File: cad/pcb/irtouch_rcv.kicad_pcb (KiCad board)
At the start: 4 copper layers, 42.8 x 43.1 mm, 106 parts, among them Q1 Q_Photo_NPN, Q10 Q_Photo_NPN, Q11 Q_Photo_NPN, Q12 Q_Photo_NPN, Q13 Q_Photo_NPN, Q14 Q_Photo_NPN, Q15 Q_Photo_NPN, Q16 Q_Photo_NPN, Q17 Q_Photo_NPN, Q18 Q_Photo_NPN, Q19 Q_Photo_NPN, Q2 Q_Photo_NPN, Q20 Q_Photo_NPN, Q21 Q_Photo_NPN, Q22 Q_Photo_NPN, Q23 Q_Photo_NPN, Q24 Q_Photo_NPN, Q25 Q_Photo_NPN, Q26 Q_Photo_NPN, Q27 Q_Photo_NPN, Q28 Q_Photo_NPN, Q29 Q_Photo_NPN, Q3 Q_Photo_NPN, Q30 Q_Photo_NPN, Q31 Q_Photo_NPN, Q32 Q_Photo_NPN, Q4 Q_Photo_NPN, Q5 Q_Photo_NPN, Q6 Q_Photo_NPN, Q7 Q_Photo_NPN, Q8 Q_Photo_NPN, Q9 Q_Photo_NPN, U1 74HC4051PW,118, U2 74HC4051PW,118, U3 74HC4051PW,118, U4 74HC4051PW,118

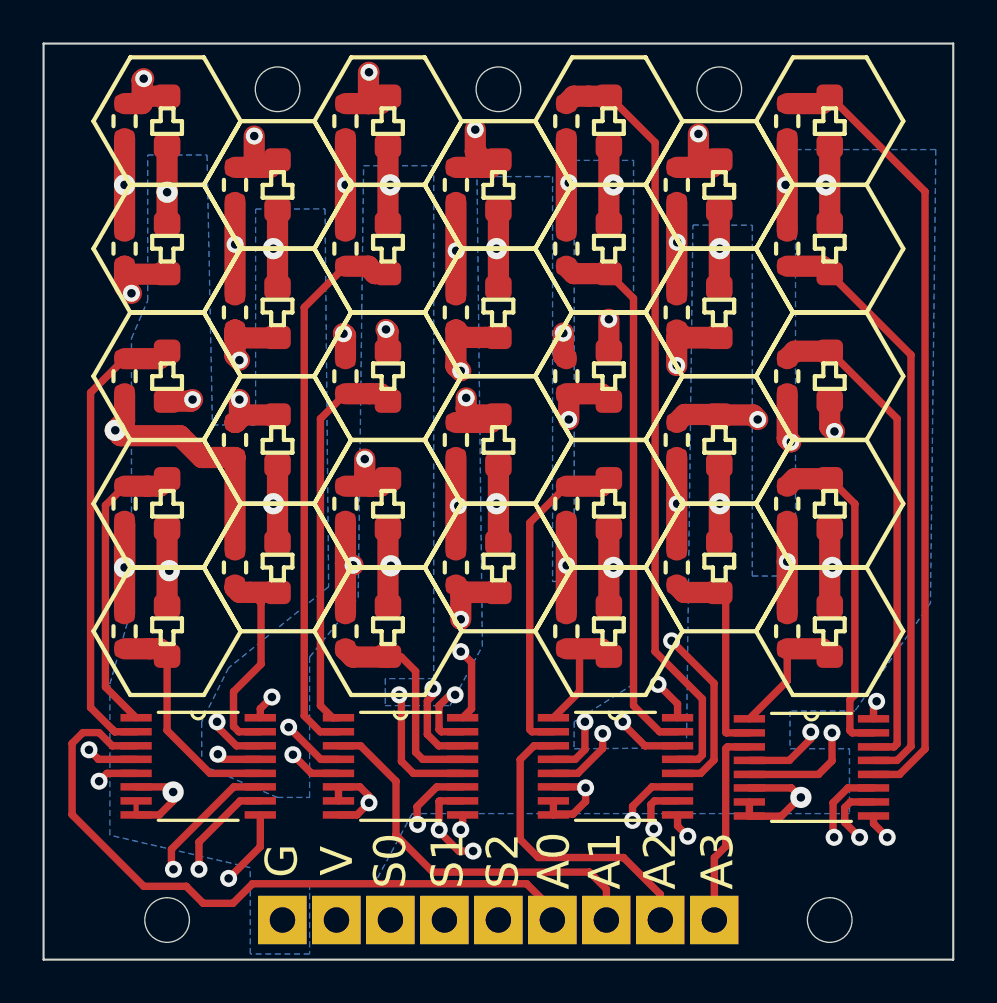
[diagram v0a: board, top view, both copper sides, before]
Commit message: added Arduino breakout pcb, updated irtouch_rcv design to 2-layer
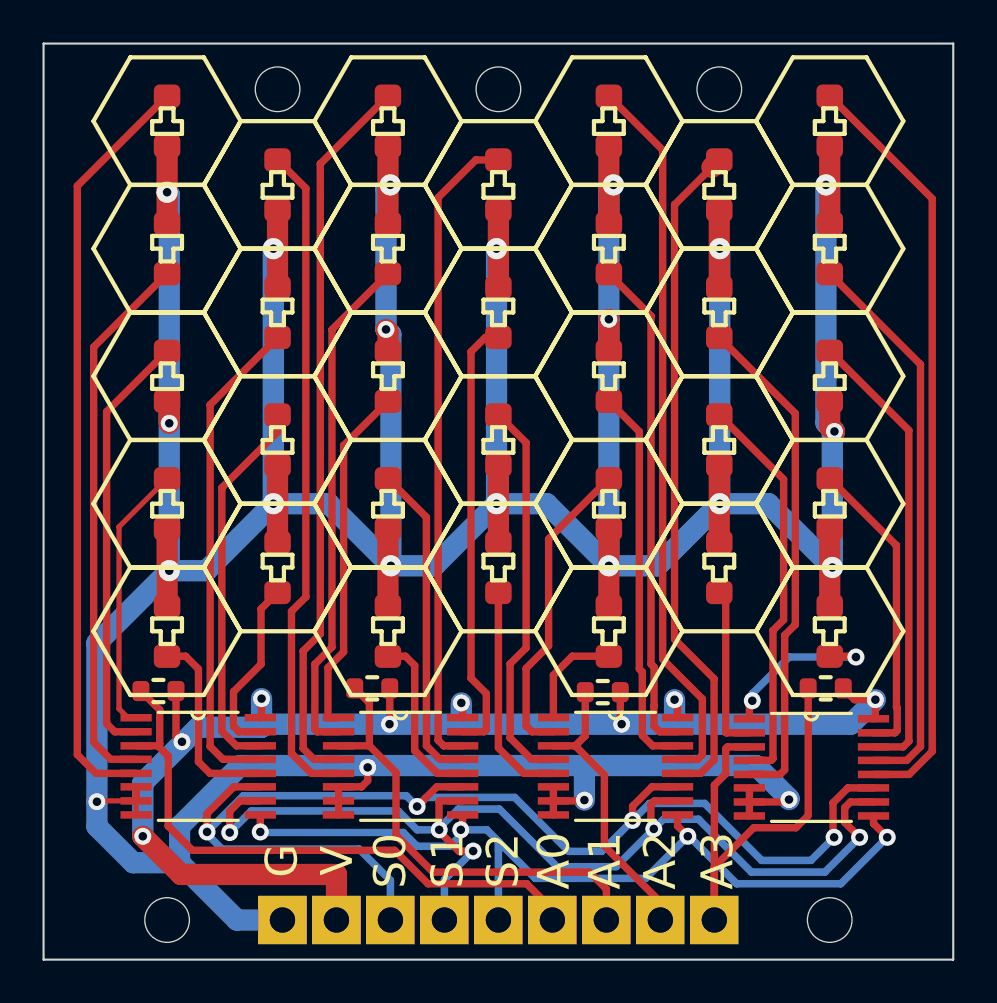
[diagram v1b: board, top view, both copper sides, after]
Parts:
- removed R10, R11, R12, R13, R14, R15, R16, R17, R18, R19, R20, R21, R22, R23, R24, R25, R26, R27, R28, R29, R30, R31, R32, R5, R6, R7, R8, R9: R, IRTouch:R0603
- moved R4 34.1 mm to (85.0, 62.7), turned to 180 degrees
- moved R3 27.0 mm to (74.5, 62.9), turned to 180 degrees
- moved R1 26.9 mm to (53.6, 62.8), turned to 180 degrees
- moved R2 23.7 mm to (63.7, 62.7), turned to 180 degrees
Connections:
- R1 pad 2: /RCV1 -> /A0
- R2 pad 2: /RCV2 -> /A1
- R3 pad 2: /RCV3 -> /A2
- R4 pad 2: /RCV4 -> /A3
- U2 pad 12: /RCV13 -> /RCV14
- U2 pad 13: /RCV14 -> /RCV13
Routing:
- net /12/24V: track 304.4 -> 65.1 mm, vias 21 -> 8
- net GND: track 76.3 -> 273.6 mm
- net /A3: track 9.43 -> 23.3 mm
- net /RCV25: track 33.3 -> 23.8 mm, vias 2 -> 0
- net /RCV18: track 17.8 -> 10.4 mm, vias 2 -> 0
- net /RCV13: track 22.7 -> 15.3 mm, vias 2 -> 0
- net /S0: track 65.3 -> 58.6 mm
- net /RCV17: track 24.8 -> 18.5 mm, vias 2 -> 0
- net /RCV6: track 37.6 -> 31.4 mm, vias 2 -> 0
- net /RCV24: track 37.7 -> 31.8 mm, vias 2 -> 0
- net /RCV15: track 36.0 -> 30.4 mm, vias 2 -> 0
- net /RCV1: track 40.9 -> 35.9 mm, vias 2 -> 0
- net /RCV10: track 39.0 -> 34.2 mm, vias 2 -> 0
- net /RCV26: track 23.4 -> 18.8 mm, vias 2 -> 0
- net /S2: track 46.6 -> 42.0 mm
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- removed copper zone on B.Cu, net GND
